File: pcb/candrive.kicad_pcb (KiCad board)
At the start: 4 copper layers, 96 x 42.2 mm, 84 parts, among them J1 Conn_01x02_Male, J2 Conn_01x06_Male, J3 Conn_01x06_Male, J4 Conn_01x06_Male, J5 Conn_01x03_Male, J6 Conn_01x06_Male, Q1 AO3401A, Q2 BC546, SW1 SW_Push, U1 STM32F103RBTx, U2 LD1117S33TR_SOT223, U3 SN65HVD234, U4 VNH7070BASTR, U5 VNH7070BASTR, U6 MAX5035BUSA

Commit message: Update PCB with new components
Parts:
- removed the C1 at (192.0, 114.3)
- removed the C2 at (201.4, 112.3)
- removed the C3 at (190.7, 136.4)
- removed the C4 at (201.2, 134.9)
- removed the C5 at (128.5, 127.8)
- removed the R2 at (192.0, 116.3)
- removed R20, R24, R25, R27, R28: 1K, Resistor_SMD:R_0805_2012Metric_Pad1.20x1.40mm_HandSolder
- removed R22, R34: 10K, Resistor_SMD:R_0805_2012Metric_Pad1.20x1.40mm_HandSolder
- removed R23: 1K5, Resistor_SMD:R_0805_2012Metric_Pad1.20x1.40mm_HandSolder
- removed R26: 47K, Resistor_SMD:R_0805_2012Metric_Pad1.20x1.40mm_HandSolder
- removed the R3 at (197.6, 112.3)
- removed R35: 1.2K, Resistor_SMD:R_0805_2012Metric_Pad1.20x1.40mm_HandSolder
- removed the R4 at (192.0, 112.3)
- removed the R5 at (192.0, 118.4)
- removed the R6 at (201.7, 121.9)
- removed the R7 at (192.0, 120.4)
- removed TP5: VSENSE, TestPoint:TestPoint_THTPad_D1.0mm_Drill0.5mm
- removed the U4 at (199.6, 117.1)
- added C18: 100n, Capacitor_SMD:C_0805_2012Metric_Pad1.18x1.45mm_HandSolder, F.Cu at (157.0, 139.2)
- added C19: 1u, Capacitor_SMD:C_0805_2012Metric_Pad1.18x1.45mm_HandSolder, F.Cu at (157.0, 142.2)
- added C20: 100n, Capacitor_SMD:C_0805_2012Metric_Pad1.18x1.45mm_HandSolder, F.Cu at (164.6, 139.4)
- added C21: 1u, Capacitor_SMD:C_0805_2012Metric_Pad1.18x1.45mm_HandSolder, F.Cu at (164.6, 142.5)
- added JP3: SolderJumper_2_Bridged, Jumper:SolderJumper-2_P1.3mm_Open_TrianglePad1.0x1.5mm, F.Cu at (175.3, 139.7)
- added U6: TLE72093RAUMA1, candrive:PG-DSO-20-65_11X15P9_INF, F.Cu at (190.5, 115.8)
- C1: renamed from C8; value 100nF -> C
- C10: renamed from C17; value 0.1uF -> C
- C12: renamed from C18; value 68uF -> C
- C13: renamed from C6; value 0.1uF -> C
- C15: renamed from C7; value 100uF -> C
- C16: renamed from C19; value 1uF -> C
- C17: renamed from C20; value 1uF -> C
- C2: renamed from C14; value 100nF -> C
- C3: renamed from C10; value 100nF -> C
- C4: renamed from C11; value 100nF -> C
- C5: renamed from C12; value 100nF -> C
- C6: renamed from C13; value 100nF -> C
- C7: renamed from C15; value 68uF -> C
- C8: renamed from C9; value 0.1uF -> C
- C9: renamed from C16; value 0.1uF -> C
- L1: value 100uH -> L
- R1: renamed from R18; value 10K -> R
- R10: renamed from R30; value 2K -> R
- R11: renamed from R21; value 2.7K -> R
- R12: renamed from R10; value 1K -> R
- R13: renamed from R11; value 1K -> R
- R14: renamed from R31; value 1K -> R
- R15: renamed from R32; value 1K -> R
- R16: renamed from R14; value 22 -> R
- R17: renamed from R15; value 22 -> R
- R18: renamed from R16; value 22 -> R
- R19: renamed from R17; value 22 -> R
- R2: renamed from R12; value 510 -> R
- R3: renamed from R13; value 1k -> R
- R4: renamed from R19; value 10K -> R
- R5: renamed from R1; value 1K -> R
- R6: renamed from R33; value 120 -> R
- R7: renamed from R8; value 2K -> R
- R8: renamed from R29; value 2K -> R
- R9: value 2K -> R
- TP1: value VCC -> TestPoint
- TP2: value 5V -> TestPoint
- TP3: value 3.3V -> TestPoint
- TP4: value ENCEN -> TestPoint
- U5: value VNH7070BASTR -> TLE72093RAUMA1; footprint andreas:VNH7070BASTR -> candrive:PG-DSO-20-65_11X15P9_INF
- moved U5 9.86 mm to (189.2, 136.4)
- moved JP1 4.01 mm to (180.0, 111.0)
- moved C3 2.34 mm to (178.3, 126.5)
- moved C4 2.34 mm to (178.3, 128.5)
- moved C6 2.34 mm to (178.3, 132.6)
- moved C5 2.34 mm to (178.3, 130.6)
- renumbered J5 to J2, J2 to J3, J6 to J4, J3 to J5, J4 to J6, U3 to U2, U6 to U3, U2 to U4
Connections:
- C15 pad 1: +3V3 -> +3.3V
- C3 pad 1: +3V3 -> +3.3V
- C4 pad 1: +3V3 -> +3.3V
- C5 pad 1: +3V3 -> +3.3V
- C6 pad 1: +3V3 -> +3.3V
- C8 pad 1: +3V3 -> +3.3V
- FB1 pad 1: +3V3 -> +3.3V
- J5 pad 3: +3V3 -> Net-(J5-Pad3)
- JP2 pad 2: +3V3 -> +3.3V
- TP3 pad 1: +3V3 -> +3.3V
- U1 pad 19: +3V3 -> +3.3V
- U1 pad 20: unconnected-(U1-Pad20) -> /CS_1
- U1 pad 21: /LED_1 -> /SCK
- U1 pad 22: unconnected-(U1-Pad22) -> /MISO
- U1 pad 23: unconnected-(U1-Pad23) -> /MOSI
- U1 pad 24: /VSENSE -> unconnected-(U1-Pad24)
- U1 pad 32: +3V3 -> +3.3V
- U1 pad 34: /SEL_2 -> /EN_2
- U1 pad 41: unconnected-(U1-Pad41) -> /CS_2
- U1 pad 42: unconnected-(U1-Pad42) -> /LED_1
- U1 pad 43: unconnected-(U1-Pad43) -> /ENCEN
- U1 pad 48: +3V3 -> +3.3V
- U1 pad 64: +3V3 -> +3.3V
- U1 pad 8: /SEL_1 -> /EN_1
- U2 pad 3: +3V3 -> +3.3V
- U3 pad 5: unconnected-(U6-Pad5) -> Net-(JP3-Pad2)
- U4 pad 2: +3V3 -> +3.3V
- U5 pad 10: /OUTA_2 -> GND
- U5 pad 11: Net-(R25-Pad2) -> GND
- U5 pad 12: VCC -> /Motor driver 2/DMS
- U5 pad 13: Net-(R22-Pad2) -> /EN_2
- U5 pad 14: Net-(R24-Pad2) -> /OUTB_2
- U5 pad 16: GND -> VCC
- U5 pad 2: /OUTA_2 -> /SCK
- U5 pad 3: Net-(R27-Pad1) -> /INA_2
- U5 pad 4: VCC -> unconnected-(U5-Pad4)
- U5 pad 6: Net-(R28-Pad1) -> /OUTA_2
- U5 pad 7: /OUTB_2 -> /OUTA_2
- U5 pad 8: GND -> /MISO
- U5 pad 9: GND -> /MOSI

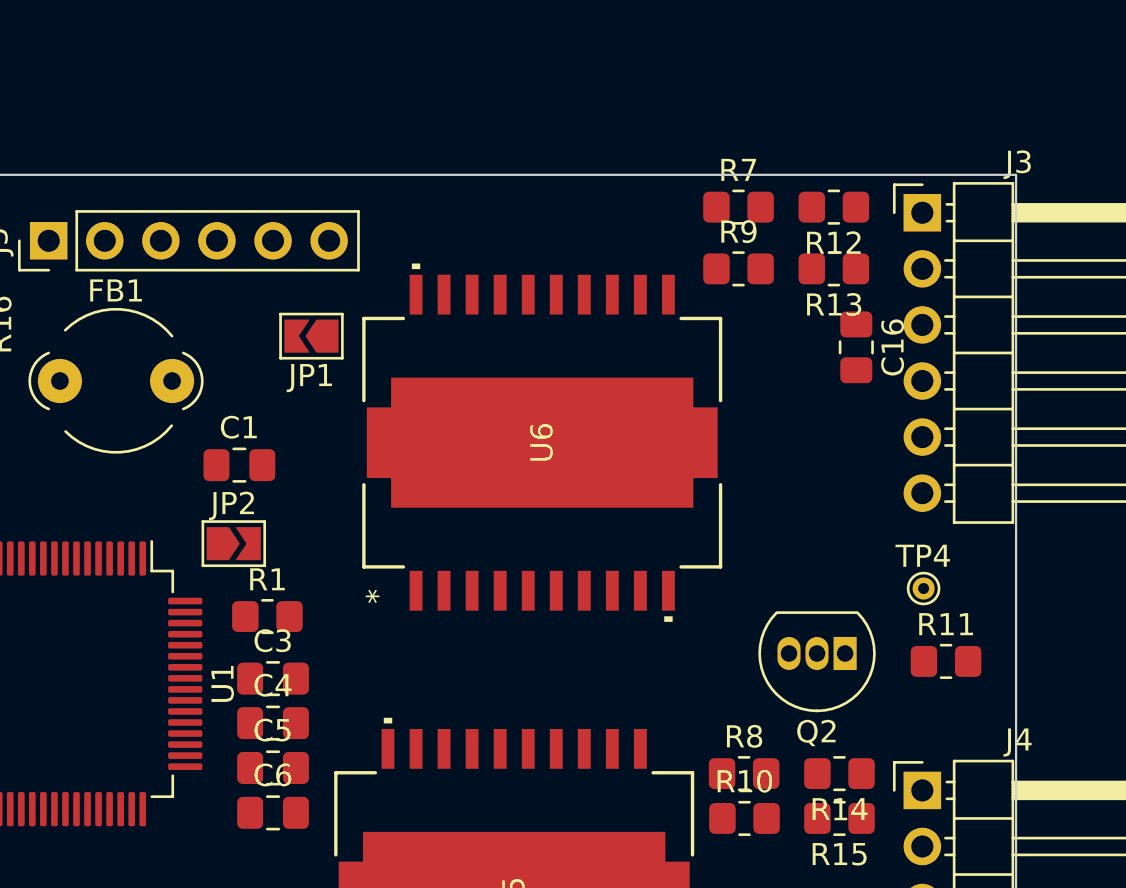
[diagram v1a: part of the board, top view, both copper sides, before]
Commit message: Add missing footprint
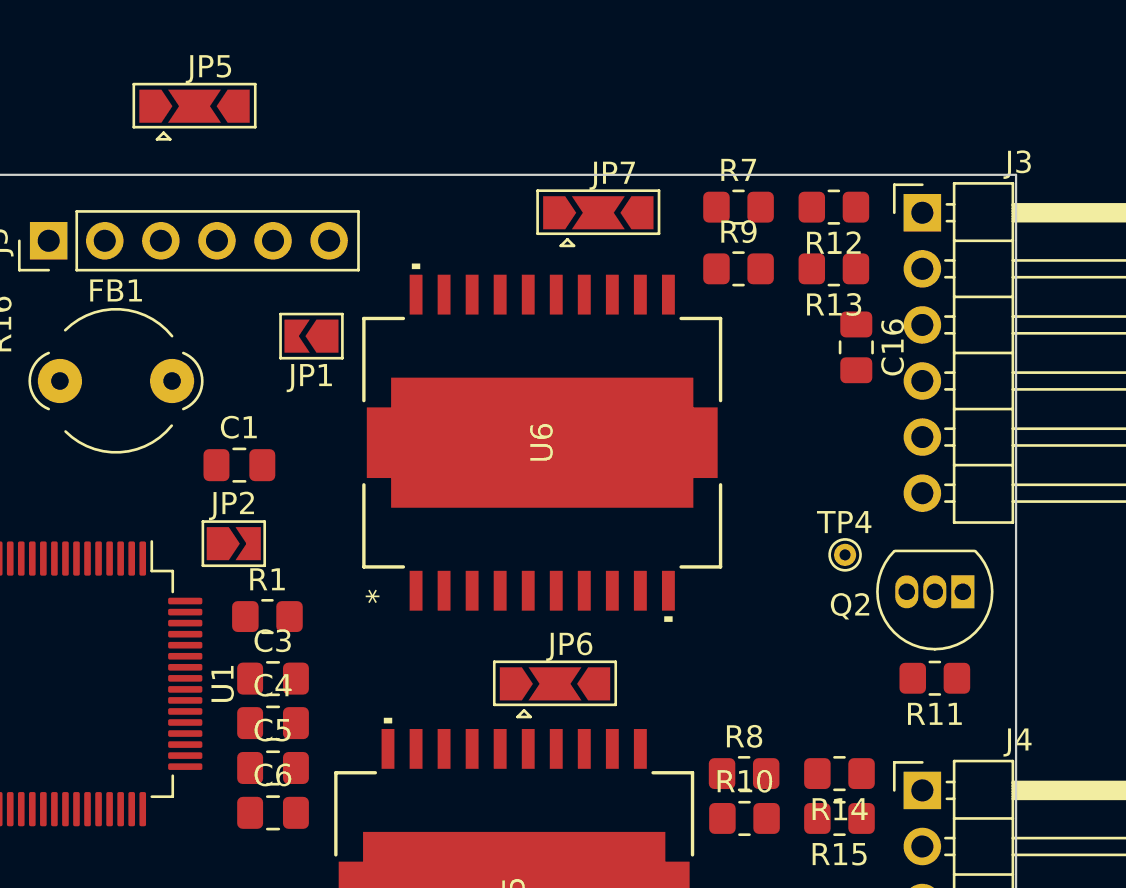
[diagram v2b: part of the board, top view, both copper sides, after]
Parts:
- added JP5: SolderJumper_3_Open, Jumper:SolderJumper-3_P2.0mm_Open_TrianglePad1.0x1.5mm, F.Cu at (174.8, 100.6)
- added JP6: SolderJumper_3_Bridged12, Jumper:SolderJumper-3_P2.0mm_Open_TrianglePad1.0x1.5mm, F.Cu at (191.1, 126.7)
- added JP7: SolderJumper_3_Bridged12, Jumper:SolderJumper-3_P2.0mm_Open_TrianglePad1.0x1.5mm, F.Cu at (193.0, 105.4)
- moved Q2 6.02 mm to (209.6, 122.6)
- moved TP4 3.87 mm to (204.2, 120.9)
- moved R11 0.92 mm to (208.3, 126.5), turned to 180 degrees
